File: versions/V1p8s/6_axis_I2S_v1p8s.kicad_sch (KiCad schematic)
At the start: 96 parts, among them J1 2 Pos, J10 8S, J11 JTAG, J12 2 Pos, J13 8S, J14 8S, J15 2 Pos, J16 8S, J17 8S, J18 6S, J19 2 Pos, J2 8S, J20 8S, J21 8S, J22 3P, J23 3P, J24 3P, J25 6S, J26 2 Pos, J27 8S, J28 8S, J3 8S, J4 19S, J5 ESP32_DEVKITC_01-19, J6 ESP32_DEVKITC_20-38, J7 19S, J8 2 Pos, J9 8S, U1 74AHCT595, U2 74AHCT595, U3 74AHCT595, U4 74AHCT595, U5 TPS54360

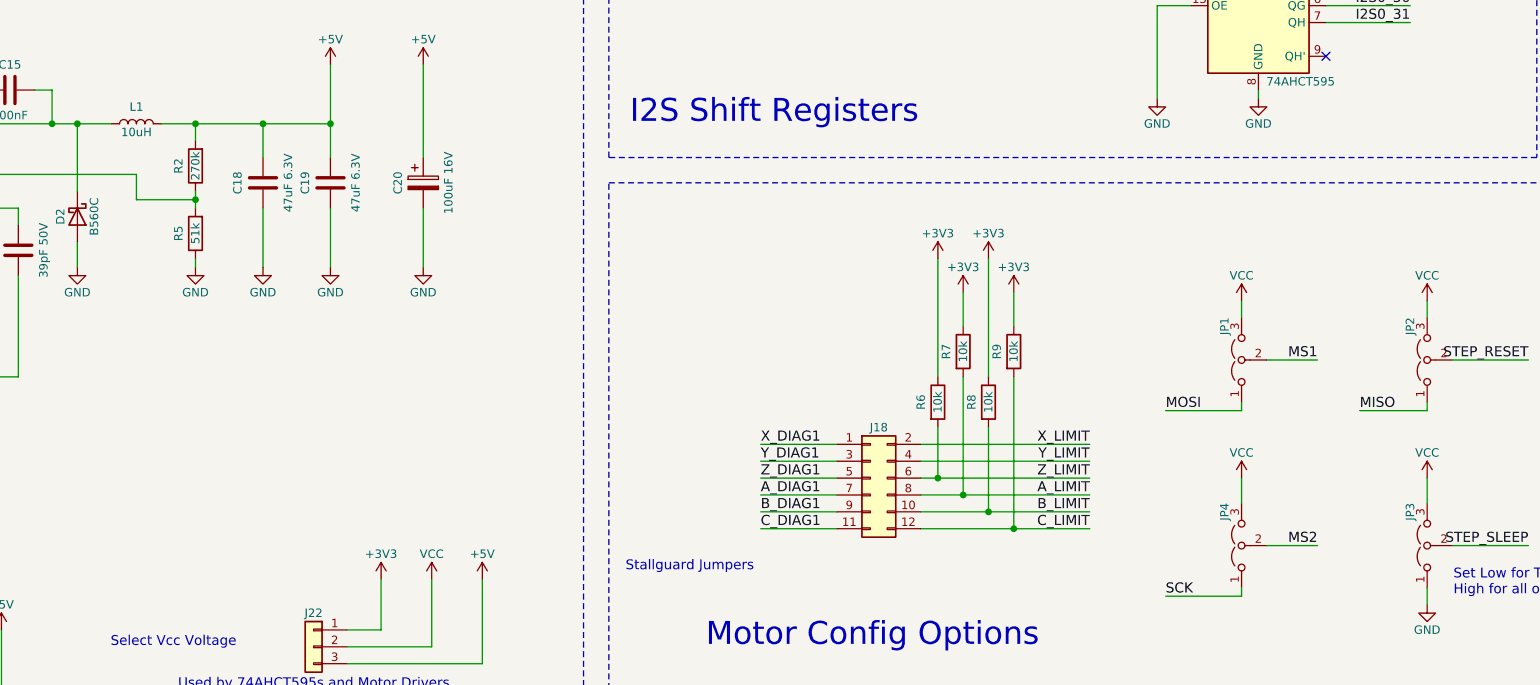
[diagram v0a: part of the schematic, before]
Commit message: layout changes, screw hole placement changes, generate gerbers
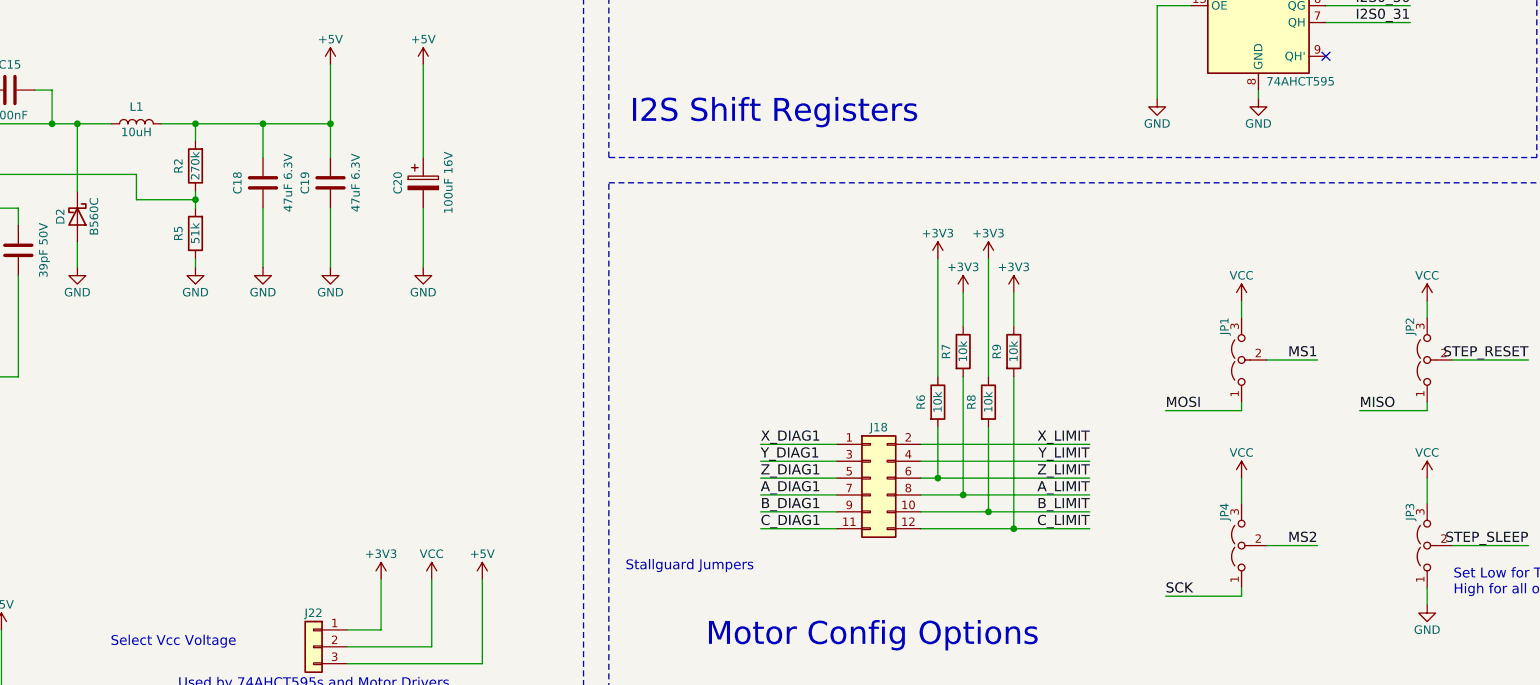
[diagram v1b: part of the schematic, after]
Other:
- note added: "~{Ena}"
- note added: "~{Rst} (SDO)"
- note added: "~{Sleep} (NC)"
- note removed: "~Ena"
- note removed: "~Rst (SDO)"
- note removed: "~Sleep (NC)"
